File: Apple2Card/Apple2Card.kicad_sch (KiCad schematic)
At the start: 77 parts, among them J1 ICSP, J2 Conn_01x25, J3 Conn_01x25, J4 Conn_01x16, J5 SERCON, J6 WIZNET 5500, SW1 SW_Push, U1 ATmega328P-P, U2 74HCT32, U3 74HCT00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

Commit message: Minor updates to PCB & schematics: - Realigned some components (LEDs etc). - Added some clearance to the slot connector (now allows production with "chamfered edges"). - Show component values on the silk screen (so no separate schematics are required when soldering) - Changed pull-down resistors for 82C55s I/O pins to 4k7 (instead of 10k), since they   were too weak to overcome the minimum current mentioned in the 8255 data sheet   (though the 10k resistors still worked with most types - but not with all). - Changed the two load resistors for the SD card supply voltage, to slightly increase the   voltage drop across the diodes. The SD supply voltage was a bit high.
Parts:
- JP10: value PG2 -> PG9
- JP8: value PG2 -> PG4
- JP9: value PG2 -> PG8
- R11, R12: value 10k -> 1k
- R18, R2, R21, R22, R23, R3, R7: value 10k -> 4k7
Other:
- note added: "APPLE II ARDUINO INTERFACE BY DANIEL MARKS, VERSION 1.1.1 CC-BY-SA 4.0"
- note removed: "APPLE II ARDUINO INTERFACE BY DANIEL MARKS, VERSION 1 CC-BY-SA 4.0"
- company: (none) -> Daniel L. Marks
- title: (none) -> DAN ][ Controller

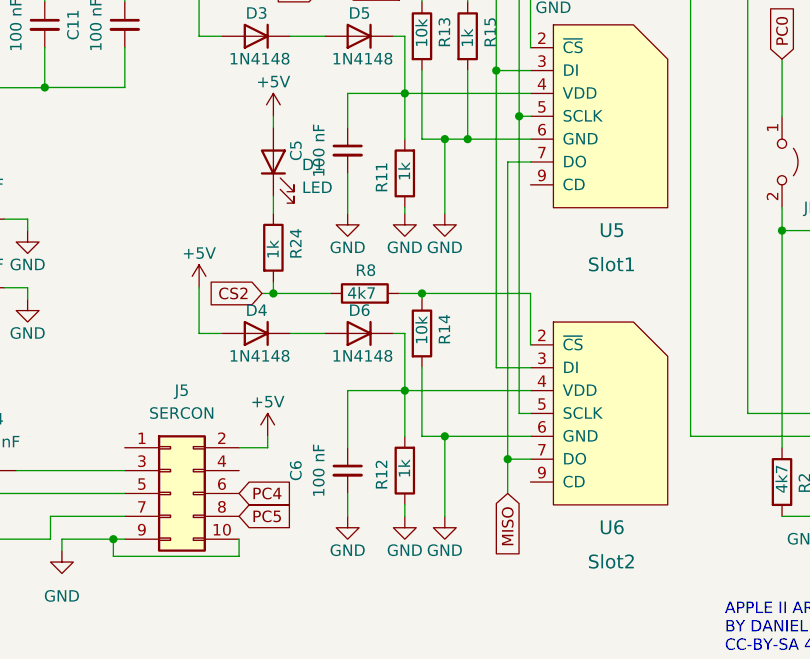
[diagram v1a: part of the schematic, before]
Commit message: Documentation updates Matched name of ATmega328 Gerber file and link in README. Adapted links in README to use relative paths. Updated PCB image. Incorporated Dan's comment concerning D7/R20: they are optional. It's recommended to close JP5, in which case D7/R20 are obsolete.
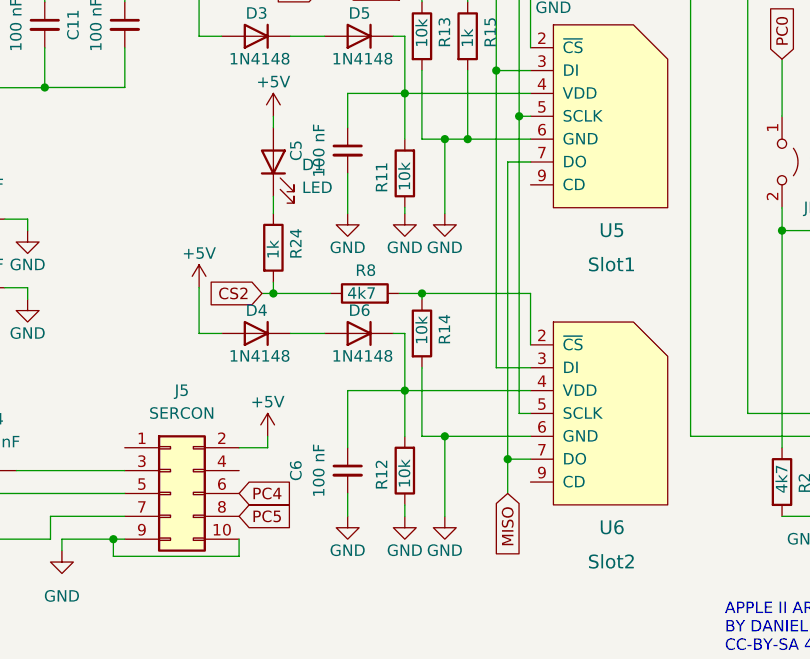
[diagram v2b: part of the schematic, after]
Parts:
- R11, R12: value 1k -> 10k
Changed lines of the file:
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@@
       (effects (font (size 1.27 1.27)) (justify left))
     )
-    (property "Value" "1k" (id 1) (at 149.86 154.94 90)
+    (property "Value" "10k" (id 1) (at 149.86 154.94 90)
       (effects (font (size 1.27 1.27)) (justify left))
     )
@@
       (effects (font (size 1.27 1.27)) (justify left))
     )
-    (property "Value" "1k" (id 1) (at 149.86 121.92 90)
+    (property "Value" "10k" (id 1) (at 149.86 121.92 90)
       (effects (font (size 1.27 1.27)) (justify left))
     )
@@
     )
     (path "/ff6e6140-2d19-4d00-a3e4-4df66358543b"
-      (reference "R11") (unit 1) (value "1k") (footprint "Resistor_THT:R_Axial_DIN0207_L6.3mm_D2.5mm_P7.62mm_Horizontal")
+      (reference "R11") (unit 1) (value "10k") (footprint "Resistor_THT:R_Axial_DIN0207_L6.3mm_D2.5mm_P7.62mm_Horizontal")
     )
     (path "/df35cae4-266a-4803-bfde-b438aa8494ef"
-      (reference "R12") (unit 1) (value "1k") (footprint "Resistor_THT:R_Axial_DIN0207_L6.3mm_D2.5mm_P7.62mm_Horizontal")
+      (reference "R12") (unit 1) (value "10k") (footprint "Resistor_THT:R_Axial_DIN0207_L6.3mm_D2.5mm_P7.62mm_Horizontal")
     )
     (path "/d8b98984-8238-4fb0-9b8d-49265f555b80"
